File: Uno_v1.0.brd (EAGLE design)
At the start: 68.6 x 53.3 mm, 61 parts, among them CN1 POWER_JACK, CN2 47346-0001, CN3 DIGITAL10, CN4 DIGITAL8, CN5 ICSP, CN6 POWER8, CN7 ANALOG6, IC1 AMS1117-5.0, IC2 AMS1117-3.3, IC3 MCP6002T-I/SN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

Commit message: Move some stuff around
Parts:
- moved C11 7.37 mm to (9.78, 23.0), turned to 0 degrees
- moved LOGO1 1.02 mm to (48.3, 8.38)
- moved R4 0.63 mm to (9.91, 31.8)
- moved R5 0.63 mm to (9.91, 30.7)
- moved T2 0.63 mm to (9.78, 19.8)
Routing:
- net VIN: track 66.8 -> 66.0 mm
- net N$12: track 8.33 -> 7.70 mm
- net 5V: track 202.9 -> 202.4 mm
- net GND: track 59.0 -> 58.9 mm, vias 254 -> 255
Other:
- board text added: "ATMega328P"

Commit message: Move stuff around
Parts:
- moved Q1 0.36 mm to (24.0, 39.9)
- moved C17 0.36 mm to (49.7, 38.4)
- moved C10 0.28 mm to (21.8, 41.9)
- moved D1 0.28 mm to (17.5, 6.10)
- moved L1 0.28 mm to (22.4, 9.14)
- moved C14 0.25 mm to (49.4, 36.6)
- moved C9 0.18 mm to (21.8, 39.0)
- moved C12 0.13 mm to (46.1, 36.8)
- moved C13 0.13 mm to (43.3, 36.8)
- moved C7 0.13 mm to (16.5, 29.2)
- moved Q2 0.13 mm to (44.8, 39.0)
- moved R5 0.13 mm to (9.91, 30.6)
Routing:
- net USB_DTR: track 48.0 -> 42.1 mm
- net D0_RX: track 98.4 -> 93.2 mm, vias 6 -> 4
- net D1_TX: track 98.1 -> 94.2 mm, vias 6 -> 4
- net GND: track 58.9 -> 60.6 mm, vias 255 -> 254
- net 5V: track 202.4 -> 201.3 mm
- net A4_SDA: track 94.1 -> 94.9 mm
- net RESET: track 130.5 -> 129.9 mm
- net D13_SCK: track 109.2 -> 108.6 mm

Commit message: Move stuff around.
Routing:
- net D13_SCK: vias 4 -> 3
- net GND: vias 254 -> 253
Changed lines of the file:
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@@
 <drawing>
 <settings>
-<setting alwaysvectorfont="yes"/>
+<setting alwaysvectorfont="no"/>
 <setting verticaltext="up"/>
 </settings>
@@
 <via x="21.463" y="23.622" extent="1-16" drill="0.35"/>
 <via x="18.669" y="23.495" extent="1-16" drill="0.35"/>
-<via x="32.258" y="18.161" extent="1-16" drill="0.35"/>
+<via x="32.258" y="18.288" extent="1-16" drill="0.35"/>
 <via x="32.258" y="20.955" extent="1-16" drill="0.35"/>
 <via x="25.527" y="18.796" extent="1-16" drill="0.35"/>
@@
 <via x="34.163" y="37.338" extent="1-16" drill="0.35"/>
 <via x="34.163" y="44.323" extent="1-16" drill="0.35"/>
-<via x="34.036" y="24.511" extent="1-16" drill="0.35"/>
+<via x="34.036" y="24.13" extent="1-16" drill="0.35"/>
 <via x="30.734" y="30.099" extent="1-16" drill="0.35"/>
 <via x="34.163" y="33.401" extent="1-16" drill="0.35"/>
@@
 <wire x1="24.892" y1="42.291" x2="24.892" y2="39.9508" width="0.3048" layer="1"/>
 <via x="18.034" y="48.133" extent="1-16" drill="0.35"/>
-<via x="30.607" y="18.796" extent="1-16" drill="0.35"/>
-<via x="30.607" y="20.828" extent="1-16" drill="0.35"/>
-<via x="35.052" y="21.082" extent="1-16" drill="0.35"/>
+<via x="30.607" y="18.288" extent="1-16" drill="0.35"/>
+<via x="30.607" y="20.955" extent="1-16" drill="0.35"/>
 <wire x1="47.625" y1="28.575" x2="48.26" y2="29.21" width="0" layer="19" extent="1-1"/>
 </signal>
@@
 <wire x1="30.48" y1="3.429" x2="31.2166" y2="4.1656" width="0.8128" layer="1"/>
 <wire x1="37.4904" y1="4.1656" x2="38.1" y2="3.556" width="0.8128" layer="1"/>
-<wire x1="46.26" y1="24.9174" x2="46.26" y2="24.083" width="0.4064" layer="1"/>
-<wire x1="46.26" y1="24.083" x2="47.229" y2="23.114" width="0.4064" layer="1"/>
+<wire x1="46.26" y1="24.9174" x2="46.26" y2="24.21" width="0.4064" layer="1"/>
+<wire x1="47.229" y1="23.241" x2="47.229" y2="23.114" width="0.4064" layer="1"/>
+<wire x1="47.229" y1="23.241" x2="46.26" y2="24.21" width="0.4064" layer="1"/>
 <wire x1="48.66" y1="33.5026" x2="48.66" y2="35.34" width="0.4064" layer="1"/>
 <wire x1="48.66" y1="35.34" x2="48.753" y2="35.433" width="0.4064" layer="1"/>
@@
 <wire x1="30.48" y1="13.97" x2="30.528" y2="13.922" width="0.8128" layer="1"/>
 <wire x1="37.084" y1="13.922" x2="30.528" y2="13.922" width="0.8128" layer="1"/>
-<wire x1="67.77" y1="13.922" x2="49.149" y2="13.922" width="0.8128" layer="1"/>
-<wire x1="49.149" y1="13.922" x2="37.084" y2="13.922" width="0.8128" layer="1"/>
+<wire x1="67.77" y1="13.922" x2="49.276" y2="13.922" width="0.8128" layer="1"/>
+<wire x1="49.276" y1="13.922" x2="37.084" y2="13.922" width="0.8128" layer="1"/>
 <wire x1="67.818" y1="13.97" x2="67.77" y2="13.922" width="0.8128" layer="1"/>
 <wire x1="67.9196" y1="29.4894" x2="67.9196" y2="14.0716" width="0.8128" layer="16"/>
@@
 <wire x1="66.929" y1="30.48" x2="66.167" y2="30.48" width="0.8128" layer="16"/>
 <wire x1="37.084" y1="15.883" x2="37.084" y2="13.922" width="0.3048" layer="1"/>
-<wire x1="48.707" y1="38.354" x2="48.707" y2="39.563" width="0.8128" layer="1"/>
-<via x="48.895" y="39.751" extent="1-16" drill="0.5"/>
-<wire x1="48.895" y1="39.751" x2="49.149" y2="39.497" width="0.8128" layer="16"/>
-<wire x1="49.149" y1="39.497" x2="49.149" y2="22.86" width="0.8128" layer="16"/>
-<via x="49.149" y="13.922" extent="1-16" drill="0.5"/>
-<wire x1="49.149" y1="22.86" x2="49.149" y2="13.922" width="0.8128" layer="16"/>
+<wire x1="48.707" y1="38.354" x2="48.707" y2="39.436" width="0.8128" layer="1"/>
+<via x="49.022" y="39.751" extent="1-16" drill="0.5"/>
+<wire x1="49.022" y1="39.751" x2="49.276" y2="39.497" width="0.8128" layer="16"/>
+<wire x1="49.276" y1="39.497" x2="49.276" y2="22.86" width="0.8128" layer="16"/>
+<via x="49.276" y="13.922" extent="1-16" drill="0.5"/>
+<wire x1="49.276" y1="22.86" x2="49.276" y2="13.922" width="0.8128" layer="16"/>
 <via x="46.228" y="22.86" extent="1-16" drill="0.5"/>
-<wire x1="46.228" y1="22.86" x2="49.149" y2="22.86" width="0.8128" layer="16"/>
+<wire x1="46.228" y1="22.86" x2="49.276" y2="22.86" width="0.8128" layer="16"/>
 <wire x1="46.228" y1="22.86" x2="46.863" y2="22.86" width="0.4064" layer="1"/>
 <wire x1="47.229" y1="23.114" x2="47.117" y2="23.114" width="0.4064" layer="1"/>
 <wire x1="47.117" y1="23.114" x2="46.863" y2="22.86" width="0.4064" layer="1"/>
-<wire x1="48.707" y1="39.563" x2="48.895" y2="39.751" width="0.8128" layer="1"/>
+<wire x1="48.707" y1="39.436" x2="49.022" y2="39.751" width="0.8128" layer="1"/>
 <via x="15.367" y="22.2" extent="1-16" drill="0.5"/>
 <wire x1="15.367" y1="22.2" x2="15.367" y2="15.9066" width="0.8128" layer="16"/>
@@
 <wire x1="24.257" y1="22.2" x2="21.361" y2="22.2" width="0.3048" layer="1"/>
 <wire x1="23.876" y1="22.2" x2="24.257" y2="22.2" width="0.3048" layer="1"/>
-<wire x1="35.56" y1="2.54" x2="34.036" y2="4.064" width="0.8128" layer="16"/>
-<wire x1="33.909" y1="22.225" x2="34.036" y2="22.098" width="0.8128" layer="16"/>
-<wire x1="34.036" y1="22.098" x2="34.036" y2="4.064" width="0.8128" layer="16"/>
-<via x="33.909" y="22.225" extent="1-16" drill="0.5"/>
-<wire x1="33.909" y1="22.225" x2="23.901" y2="22.225" width="0.8128" layer="1"/>
+<wire x1="35.56" y1="2.54" x2="34.163" y2="3.937" width="0.8128" layer="16"/>
+<wire x1="34.163" y1="22.225" x2="34.163" y2="3.937" width="0.8128" layer="16"/>
+<via x="34.163" y="22.225" extent="1-16" drill="0.5"/>
+<wire x1="34.163" y1="22.225" x2="23.901" y2="22.225" width="0.8128" layer="1"/>
 <wire x1="23.901" y1="22.225" x2="23.876" y2="22.2" width="0.8128" layer="1"/>
 <wire x1="15.24875" y1="25.6222" x2="15.21695" y2="25.654" width="0.3048" layer="1"/>
@@
 <via x="32.258" y="23.237" extent="1-16" drill="0.35"/>
 <wire x1="47.229" y1="21.717" x2="46.975" y2="21.463" width="0.3048" layer="1"/>
-<wire x1="46.975" y1="21.463" x2="35.869975" y2="21.463" width="0.3048" layer="1"/>
-<wire x1="35.869975" y1="21.463" x2="34.222975" y2="23.11" width="0.3048" layer="1"/>
-<wire x1="34.222975" y1="23.11" x2="32.385" y2="23.11" width="0.3048" layer="1"/>
+<wire x1="46.975" y1="21.463" x2="35.996975" y2="21.463" width="0.3048" layer="1"/>
+<wire x1="35.996975" y1="21.463" x2="34.349975" y2="23.11" width="0.3048" layer="1"/>
+<wire x1="34.349975" y1="23.11" x2="32.385" y2="23.11" width="0.3048" layer="1"/>
 <wire x1="32.385" y1="23.11" x2="32.258" y2="23.237" width="0.3048" layer="1"/>
 <wire x1="32.258" y1="23.237" x2="32.258" y2="42.672" width="0.3048" layer="16"/>
@@
 <contactref element="CN7" pad="6"/>
 <contactref element="U2" pad="23"/>
-<wire x1="50.26" y1="24.9174" x2="50.26" y2="23.463" width="0.3048" layer="1"/>
-<wire x1="50.26" y1="23.463" x2="50.165" y2="23.368" width="0.3048" layer="1"/>
-<via x="50.165" y="23.368" extent="1-16" drill="0.35"/>
-<wire x1="50.165" y1="23.368" x2="50.165" y2="3.175" width="0.3048" layer="16"/>
-<wire x1="50.165" y1="3.175" x2="50.8" y2="2.54" width="0.3048" layer="16"/>
+<wire x1="50.26" y1="24.9174" x2="50.26" y2="23.399996875" width="0.3048" layer="1"/>
+<wire x1="50.26" y1="23.399996875" x2="50.292" y2="23.368" width="0.3048" layer="1"/>
+<via x="50.292" y="23.368" extent="1-16" drill="0.35"/>
+<wire x1="50.292" y1="23.368" x2="50.292" y2="3.048" width="0.3048" layer="16"/>
+<wire x1="50.292" y1="3.048" x2="50.8" y2="2.54" width="0.3048" layer="16"/>
 <contactref element="U3" pad="19"/>
 <wire x1="50.26" y1="25.5180125" x2="49.8446125" y2="25.9334" width="0.254" layer="1"/>
@@
 <wire x1="45.46" y1="24.9174" x2="45.46" y2="24.5364" width="0.3048" layer="1"/>
 <wire x1="45.46" y1="24.5364" x2="45.1806" y2="24.257" width="0.3048" layer="1"/>
-<wire x1="45.1806" y1="24.257" x2="37.719" y2="24.257" width="0.3048" layer="1"/>
+<wire x1="45.1806" y1="24.257" x2="35.306" y2="24.257" width="0.3048" layer="1"/>
 <via x="35.306" y="24.257" extent="1-16" drill="0.35"/>
-<wire x1="37.719" y1="24.257" x2="35.306" y2="24.257" width="0.3048" layer="1"/>
 <wire x1="35.306" y1="24.257" x2="35.306" y2="44.704" width="0.3048" layer="16"/>
 <wire x1="35.306" y1="44.704" x2="29.21" y2="50.8" width="0.3048" layer="16"/>
-<wire x1="62.865" y1="19.939" x2="37.719" y2="19.939" width="0.3048" layer="1"/>
-<via x="37.719" y="19.939" extent="1-16" drill="0.35"/>
-<wire x1="37.719" y1="19.939" x2="37.719" y2="24.257" width="0.3048" layer="16"/>
-<via x="37.719" y="24.257" extent="1-16" drill="0.35"/>
-<wire x1="37.719" y1="19.939" x2="11.702" y2="19.939" width="0.3048" layer="1"/>
+<wire x1="62.865" y1="19.939" x2="35.306" y2="19.939" width="0.3048" layer="1"/>
+<wire x1="35.306" y1="19.939" x2="11.702" y2="19.939" width="0.3048" layer="1"/>
 <wire x1="11.702" y1="19.939" x2="10.729" y2="20.912" width="0.3048" layer="1"/>
 <contactref element="U3" pad="15"/>
@@
 <wire x1="45.46" y1="25.521" x2="45.46" y2="24.9174" width="0.254" layer="1"/>
 <wire x1="46.91" y1="26.717" x2="46.101" y2="25.908" width="0.254" layer="1"/>
+<wire x1="35.306" y1="24.257" x2="35.306" y2="19.939" width="0.3048" layer="16"/>
+<via x="35.306" y="19.939" extent="1-16" drill="0.35"/>
 </signal>
 <signal name="RESET">

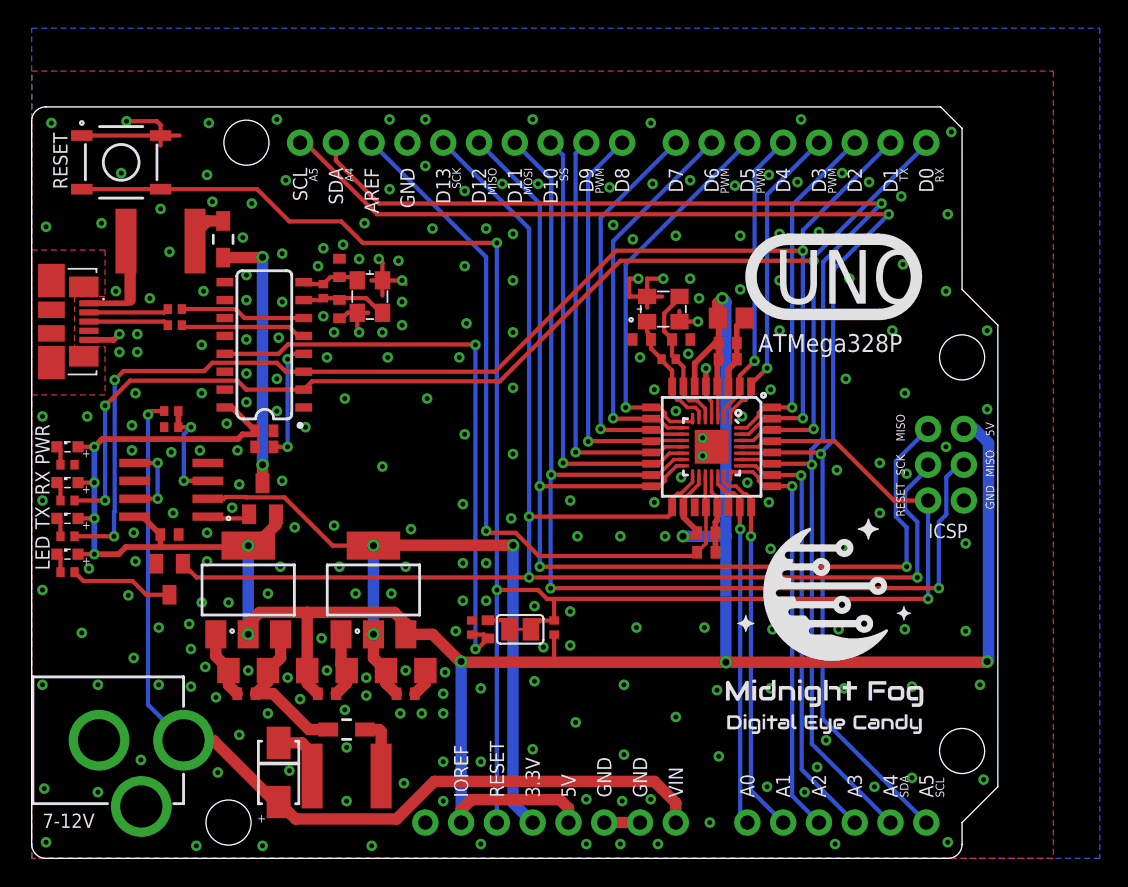
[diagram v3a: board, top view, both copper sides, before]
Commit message: Add RSN URL to the board. Moved DTR-reset group closed to CH340G.
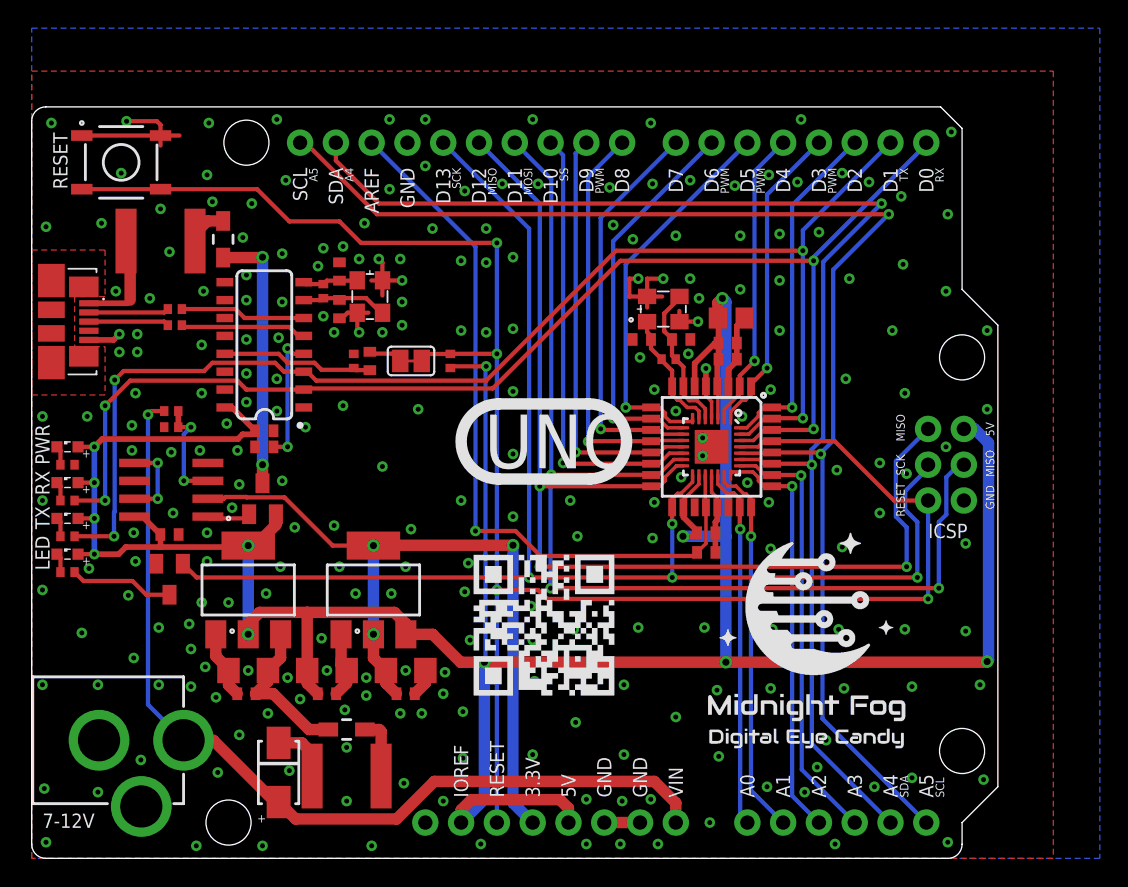
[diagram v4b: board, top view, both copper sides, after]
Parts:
- added LOGO3: RSNURL_QR_10MM, _my_logos:RSNURL_QR_10MM
- moved C18 20.8 mm to (24.0, 35.3)
- moved R11 20.7 mm to (22.9, 35.3)
- moved SJ1 20.6 mm to (26.9, 35.3)
- moved R12 20.3 mm to (29.7, 35.3)
- moved LOGO1 1.63 mm to (47.0, 7.37)
- moved LOGO2 0.52 mm to (78.7, -2.54)
- moved C10 0.25 mm to (21.8, 41.7)
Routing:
- net USB_DTR: track 42.1 -> 10.9 mm, vias 2 -> 0
- net 5V: track 201.5 -> 223.8 mm, vias 11 -> 12
- net D13_SCK: track 108.6 -> 103.0 mm, vias 3 -> 4
- net RESET: track 129.9 -> 131.9 mm, vias 3 -> 4
- net N$6: track 8.53 -> 9.29 mm
- net D1_TX: track 94.2 -> 94.7 mm
- net GND: track 60.6 -> 60.3 mm, vias 253 -> 245
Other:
- board text removed: "ATMega328P"

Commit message: Added CAM, BOM and PaP files for JLCPCB. Move some stuff around.
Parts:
- moved LOGO3 0.28 mm to (31.6, 11.7)
- moved C16 0.13 mm to (47.9, 23.0)
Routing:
- net 5V: track 223.8 -> 216.6 mm
- net GND: vias 245 -> 244
